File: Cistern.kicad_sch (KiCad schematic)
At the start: 15 parts, among them J2 Gauge Stepper, J3 Power Connector, Q1 IRF9540N, SW1 WiFi reset switch, SW2 Water Sensor, U1 ULN2003A, U3 Boost Converter (5->20 V)

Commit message: Changing schematic to fit parts and starting PCB design
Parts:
- removed Q1: IRF9540N, Package_TO_SOT_THT:TO-220-3_Vertical, symbol Transistor_FET:IRF9540N
- added Q1: BD244C, Package_TO_SOT_THT:TO-220-3_Vertical, symbol Device:Q_PNP_BCE
- D1: footprint LED_THT:LED_D4.0mm -> LED_THT:LED_D5.0mm
- R1: value 250 -> 150
- R2: value 200k -> 68
- R4: value 160 -> 150
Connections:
- net +5V: now also U1.9 (COM), Q1.3 (E); no longer R2.1
- net GND: no longer U1.9 (COM)
- net at J2.1 (Pin_1): now also U1.15 (O2); no longer U1.16 (O1)
- net at J2.2 (Pin_2): now also U1.14 (O3); no longer U1.15 (O2)
- net at J2.3 (Pin_3): now also U1.13 (O4); no longer U1.14 (O3)
- net at J2.4 (Pin_4): now also U1.12 (O5); no longer U1.13 (O4)
- net at U1.1 (I1): now also MCU1.5 (GPIO35); no longer MCU1.10 (GPIO27)
- net at D1.1 (K), R3.1: now also U1.11 (O6); no longer U1.10 (O7)
- net at R2.2: now also U1.16 (O1); no longer U1.11 (O6)
- net at U1.2 (I2): now also MCU1.6 (GPIO32); no longer MCU1.9 (GPIO26)
- net at U1.3 (I3): now also MCU1.7 (GPIO33); no longer MCU1.8 (GPIO25)
- net at U1.4 (I4): now also MCU1.8 (GPIO25); no longer MCU1.7 (GPIO33)
- net at U1.5 (I5): now also MCU1.9 (GPIO26)
- net at U1.6 (I6): now also MCU1.10 (GPIO27); no longer MCU1.6 (GPIO32)
- net at U1.7 (I7): no longer MCU1.5 (GPIO35)
- net at U3.2 (SW): now also Q1.2 (C)
- new net: Q1.1 (B), R2.1
- no-connect marks 0 -> 20
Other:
- moved on the sheet: D1, J2, R3, R4

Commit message: Working on board layout
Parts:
- removed R3: Alarm Buzzer, symbol Device:R
- added BZ1: Buzzer, Cistern:AZDelivery_KY-012_Buzzer, symbol Device:Buzzer
- D2, SW2: footprint TerminalBlock:TerminalBlock_bornier-2_P5.08mm -> Connector_PinHeader_2.54mm:PinHeader_1x02_P2.54mm_Vertical
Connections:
- net +5V: now also BZ1.1 (+)
- net at D1.1 (K), U1.11 (O6): now also BZ1.2 (-)
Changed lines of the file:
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@@
 	(wire
 		(pts
-			(xy 142.24 82.55) (xy 132.08 82.55)
+			(xy 132.08 81.28) (xy 143.51 81.28)
 		)
 		(stroke
@@
 	(wire
 		(pts
-			(xy 132.08 82.55) (xy 132.08 76.2)
+			(xy 132.08 81.28) (xy 132.08 76.2)
 		)
 		(stroke
@@
 	(wire
 		(pts
-			(xy 160.02 82.55) (xy 160.02 76.2)
+			(xy 160.02 81.28) (xy 160.02 76.2)
 		)
 		(stroke
@@
 	(wire
 		(pts
+			(xy 148.59 81.28) (xy 160.02 81.28)
+		)
+		(stroke
+			(width 0)
+			(type default)
+		)
+	)
+	(wire
+		(pts
 			(xy 110.49 105.41) (xy 96.52 105.41)
 		)
@@
 		(pts
 			(xy 191.77 110.49) (xy 191.77 107.95)
-		)
-		(stroke
-			(width 0)
-			(type default)
-		)
-	)
-	(wire
-		(pts
-			(xy 149.86 82.55) (xy 160.02 82.55)
 		)
 		(stroke
@@
 			)
 		)
-		(property "Footprint" "TerminalBlock:TerminalBlock_bornier-2_P5.08mm"
+		(property "Footprint" "Connector_PinHeader_2.54mm:PinHeader_1x02_P2.54mm_Vertical"
 			(at 162.56 125.73 0)
 			(effects
@@
 	)
 	(symbol
+		(lib_id "Device:Buzzer")
+		(at 146.05 83.82 270)
+		(unit 1)
+		(exclude_from_sim no)
+		(in_bom yes)
+		(on_board yes)
+		(dnp no)
+		(fields_autoplaced yes)
+		(property "Reference" "BZ1"
+			(at 149.86 83.305 90)
+			(effects
+				(font
+					(size 1.27 1.27)
+				)
+				(justify left)
+			)
+		)
+		(property "Value" "Buzzer"
+			(at 149.86 85.845 90)
+			(effects
+				(font
+					(size 1.27 1.27)
+				)
+				(justify left)
+			)
+		)
+		(property "Footprint" "Cistern:AZDelivery_KY-012_Buzzer"
+			(at 148.59 83.185 90)
+			(effects
+				(font
+					(size 1.27 1.27)
+				)
+				(hide yes)
+			)
+		)
+		(property "Datasheet" "~"
+			(at 148.59 83.185 90)
+			(effects
+				(font
+					(size 1.27 1.27)
+				)
+				(hide yes)
+			)
+		)
+		(property "Description" "Buzzer, polarized"
+			(at 146.05 83.82 0)
+			(effects
+				(font
+					(size 1.27 1.27)
+				)
+				(hide yes)
+			)
+		)
+		(pin "1"
+		)
+		(pin "2"
+		)
+		(instances
+			(project ""
+				(path "/387a1b1b-4d04-4a4f-a341-bb26b6058549"
+					(reference "BZ1")
+					(unit 1)
+				)
+			)
+		)
+	)
+	(symbol
 		(lib_id "Connector:Jack-DC")
 		(at 54.61 163.83 90)
@@
 			)
 		)
-		(property "Footprint" "TerminalBlock:TerminalBlock_bornier-2_P5.08mm"
+		(property "Footprint" "Connector_PinHeader_2.54mm:PinHeader_1x02_P2.54mm_Vertical"
 			(at 191.77 104.013 0)
 			(effects
@@
 					(unit 1)
 				)
-			)
-		)
-	)
-	(symbol
-		(lib_id "Device:R")
-		(at 146.05 82.55 90)
-		(mirror x)
-		(unit 1)
-		(exclude_from_sim no)
-		(in_bom yes)
-		(on_board yes)
-		(dnp no)
-		(property "Reference" "R3"
-			(at 146.05 88.9 90)
-			(effects
-				(font
-					(size 1.27 1.27)
-				)
-			)
-		)
-		(property "Value" "Alarm Buzzer"
-			(at 146.05 86.36 90)
-			(effects
-				(font
-					(size 1.27 1.27)
-				)
-			)
-		)
-		(property "Footprint" ""
-			(at 146.05 80.772 90)
-			(effects
-				(font
-					(size 1.27 1.27)
-				)
-				(hide yes)
-			)
-		)
-		(property "Datasheet" "~"
-			(at 146.05 82.55 0)
-			(effects
-				(font
-					(size 1.27 1.27)
-				)
-				(hide yes)
-			)
-		)
-		(property "Description" "Resistor"
-			(at 146.05 82.55 0)
-			(effects
-				(font
-					(size 1.27 1.27)
-				)
-				(hide yes)
-			)
-		)
-		(pin "1"
-		)
-		(pin "2"
-		)
-		(instances
-			(project ""
-				(path "/387a1b1b-4d04-4a4f-a341-bb26b6058549"
-					(reference "R3")
-					(unit 1)
-				)

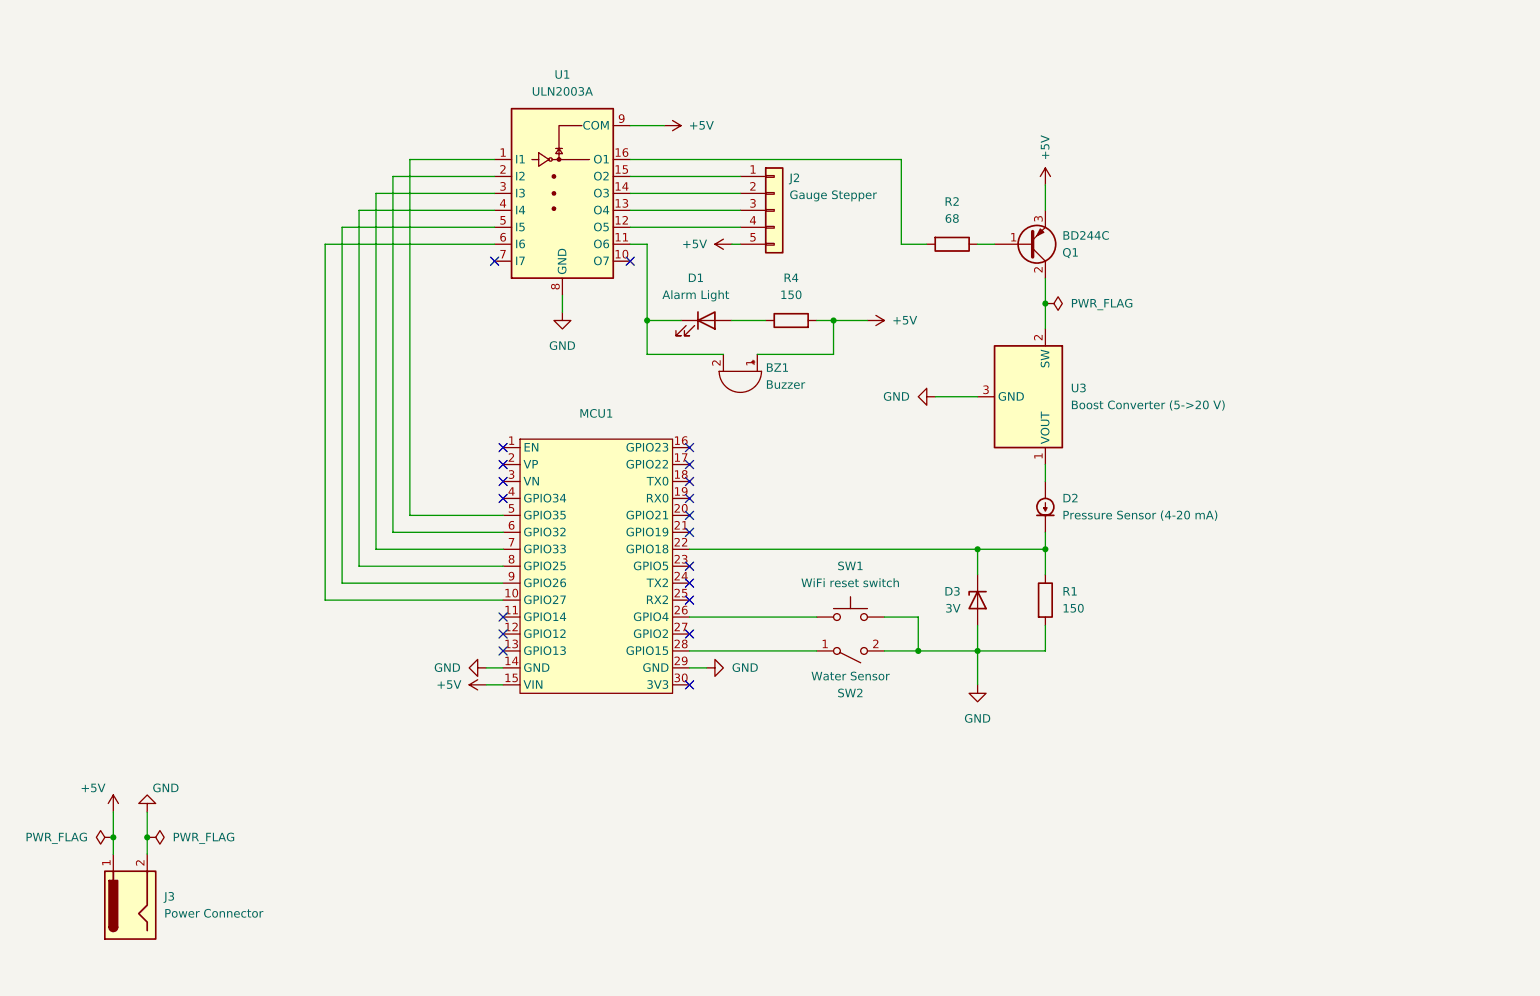
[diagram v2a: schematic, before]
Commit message: Finishing hole-grid ready PCB design
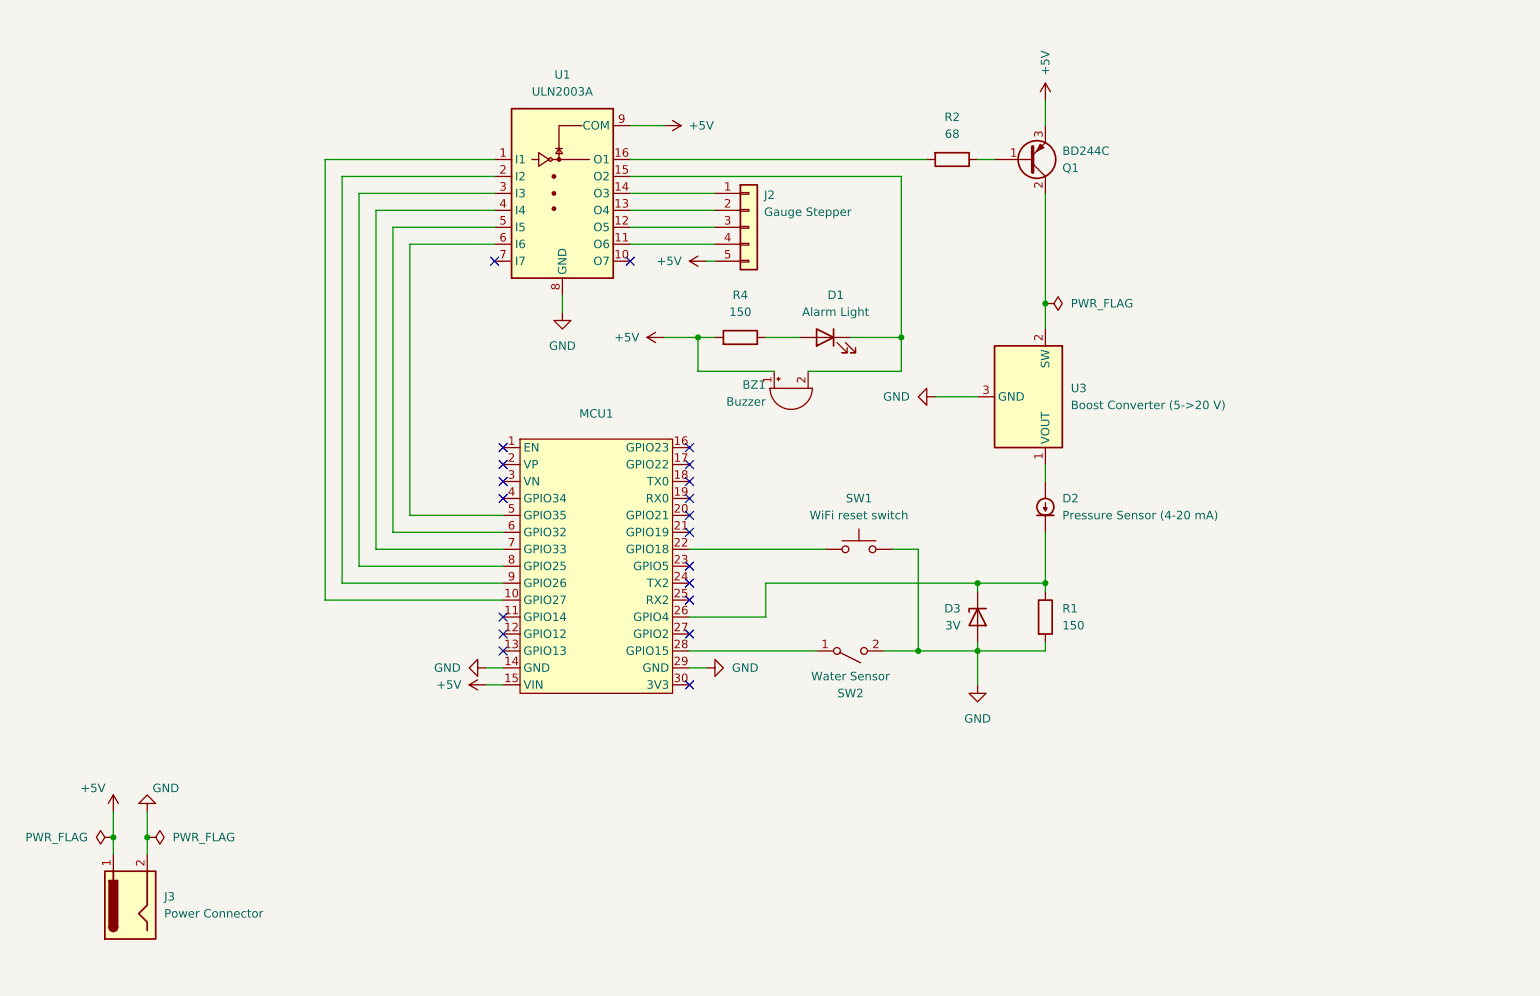
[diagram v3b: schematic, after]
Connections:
- net at J2.1 (Pin_1): now also U1.14 (O3); no longer U1.15 (O2)
- net at J2.2 (Pin_2): now also U1.13 (O4); no longer U1.14 (O3)
- net at J2.3 (Pin_3): now also U1.12 (O5); no longer U1.13 (O4)
- net at J2.4 (Pin_4): now also U1.11 (O6); no longer U1.12 (O5)
- net at U1.1 (I1): now also MCU1.10 (GPIO27); no longer MCU1.5 (GPIO35)
- net at BZ1.2 (-), D1.1 (K): now also U1.15 (O2); no longer U1.11 (O6)
- net at U1.2 (I2): now also MCU1.9 (GPIO26); no longer MCU1.6 (GPIO32)
- net at U1.3 (I3): now also MCU1.8 (GPIO25); no longer MCU1.7 (GPIO33)
- net at U1.4 (I4): now also MCU1.7 (GPIO33); no longer MCU1.8 (GPIO25)
- net at U1.5 (I5): now also MCU1.6 (GPIO32); no longer MCU1.9 (GPIO26)
- net at U1.6 (I6): now also MCU1.5 (GPIO35); no longer MCU1.10 (GPIO27)
- net at D2.1 (K), D3.1 (K), R1.1: now also MCU1.26 (GPIO4); no longer MCU1.22 (GPIO18)
- net at SW1.1: now also MCU1.22 (GPIO18); no longer MCU1.26 (GPIO4)
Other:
- moved on the sheet: BZ1, D1, D3, J2, Q1, R1, R2, R4, SW1

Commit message: Changing pin assignments to make things work
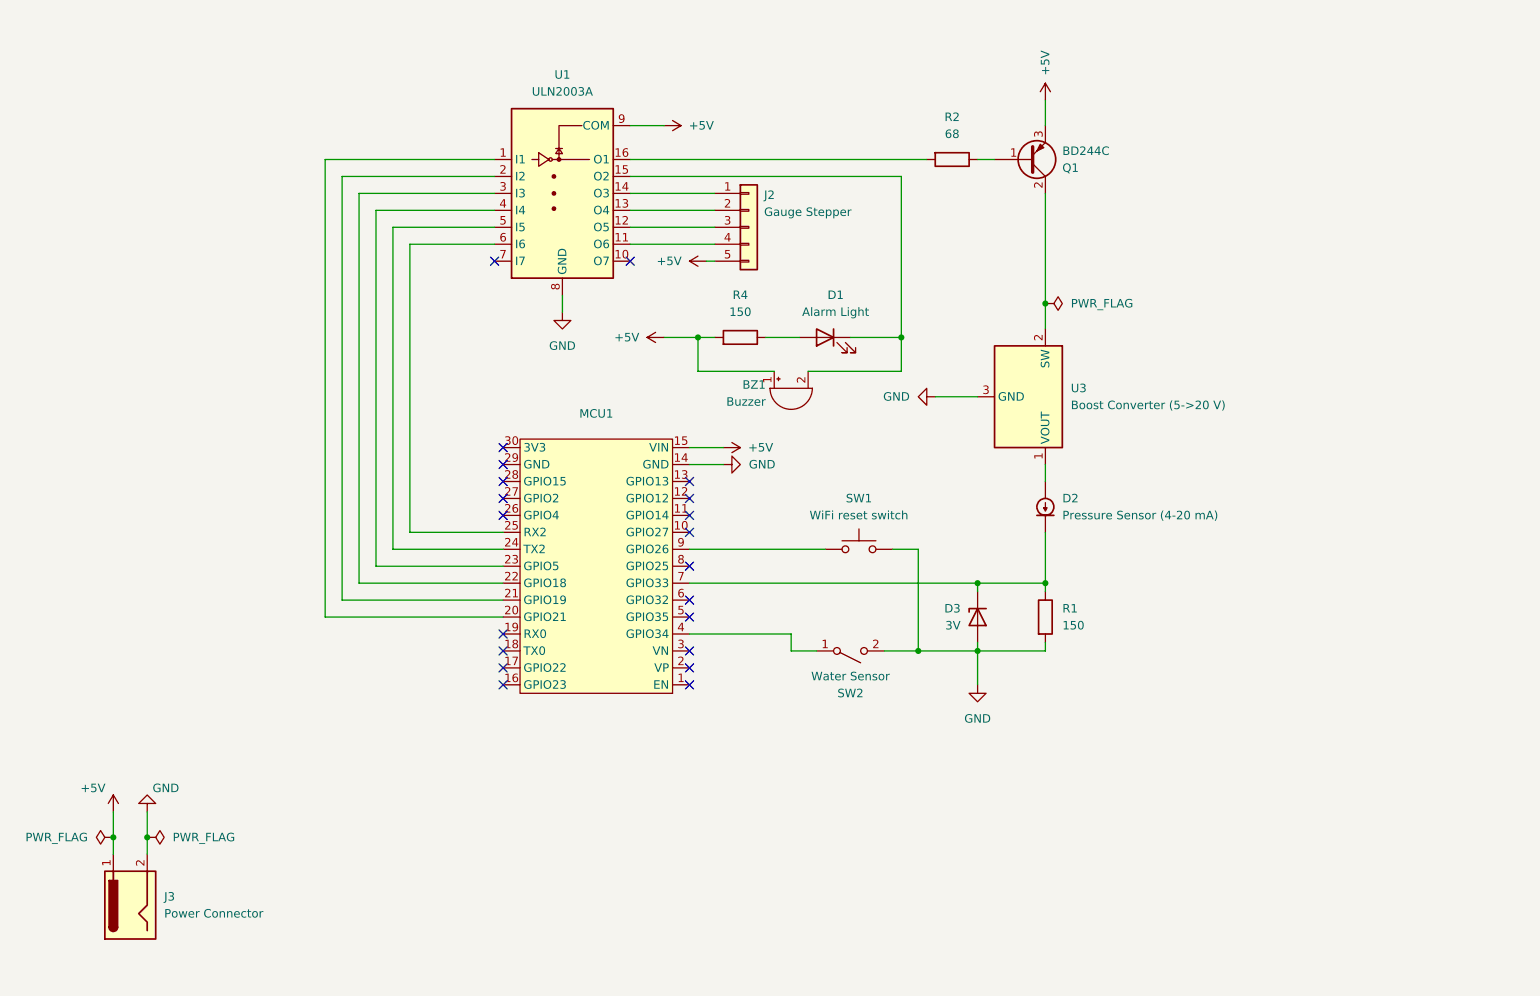
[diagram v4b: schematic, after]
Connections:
- net GND: no longer MCU1.29 (GND)
- net at U1.1 (I1): now also MCU1.20 (GPIO21); no longer MCU1.10 (GPIO27)
- net at U1.2 (I2): now also MCU1.21 (GPIO19); no longer MCU1.9 (GPIO26)
- net at U1.3 (I3): now also MCU1.22 (GPIO18); no longer MCU1.8 (GPIO25)
- net at U1.4 (I4): now also MCU1.23 (GPIO5); no longer MCU1.7 (GPIO33)
- net at U1.5 (I5): now also MCU1.24 (TX2); no longer MCU1.6 (GPIO32)
- net at U1.6 (I6): now also MCU1.25 (RX2); no longer MCU1.5 (GPIO35)
- net at SW1.1: now also MCU1.9 (GPIO26); no longer MCU1.22 (GPIO18)
- net at D2.1 (K), D3.1 (K), R1.1: now also MCU1.7 (GPIO33); no longer MCU1.26 (GPIO4)
- net at MCU1.28 (GPIO15): no longer SW2.1 (A)
- net at MCU1.4 (GPIO34): now also SW2.1 (A)
- no-connect marks 20 -> 21
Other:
- moved on the sheet: MCU1

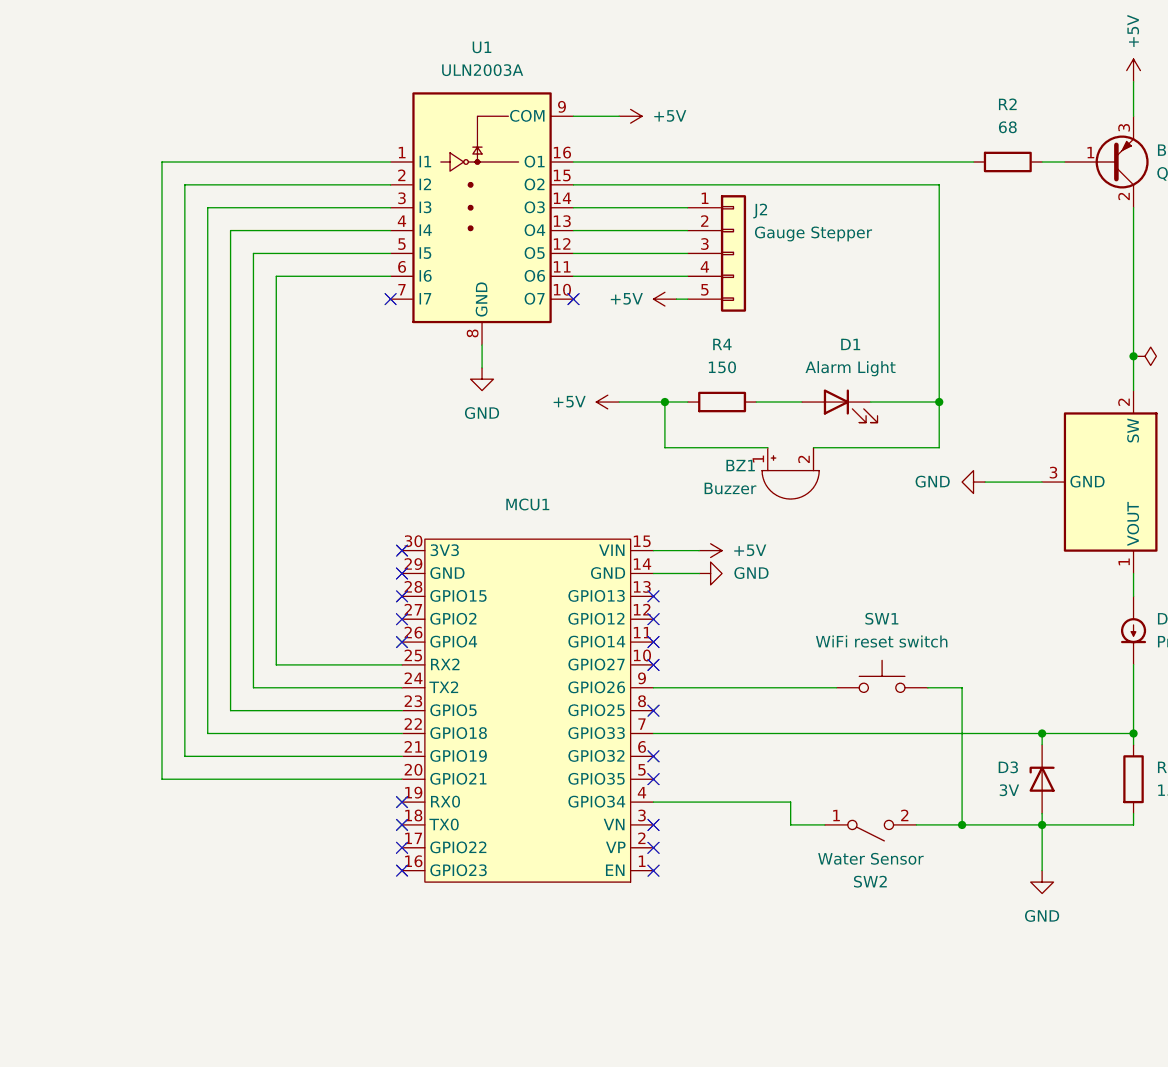
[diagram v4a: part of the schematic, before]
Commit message: Changing assignments some more and updating board design
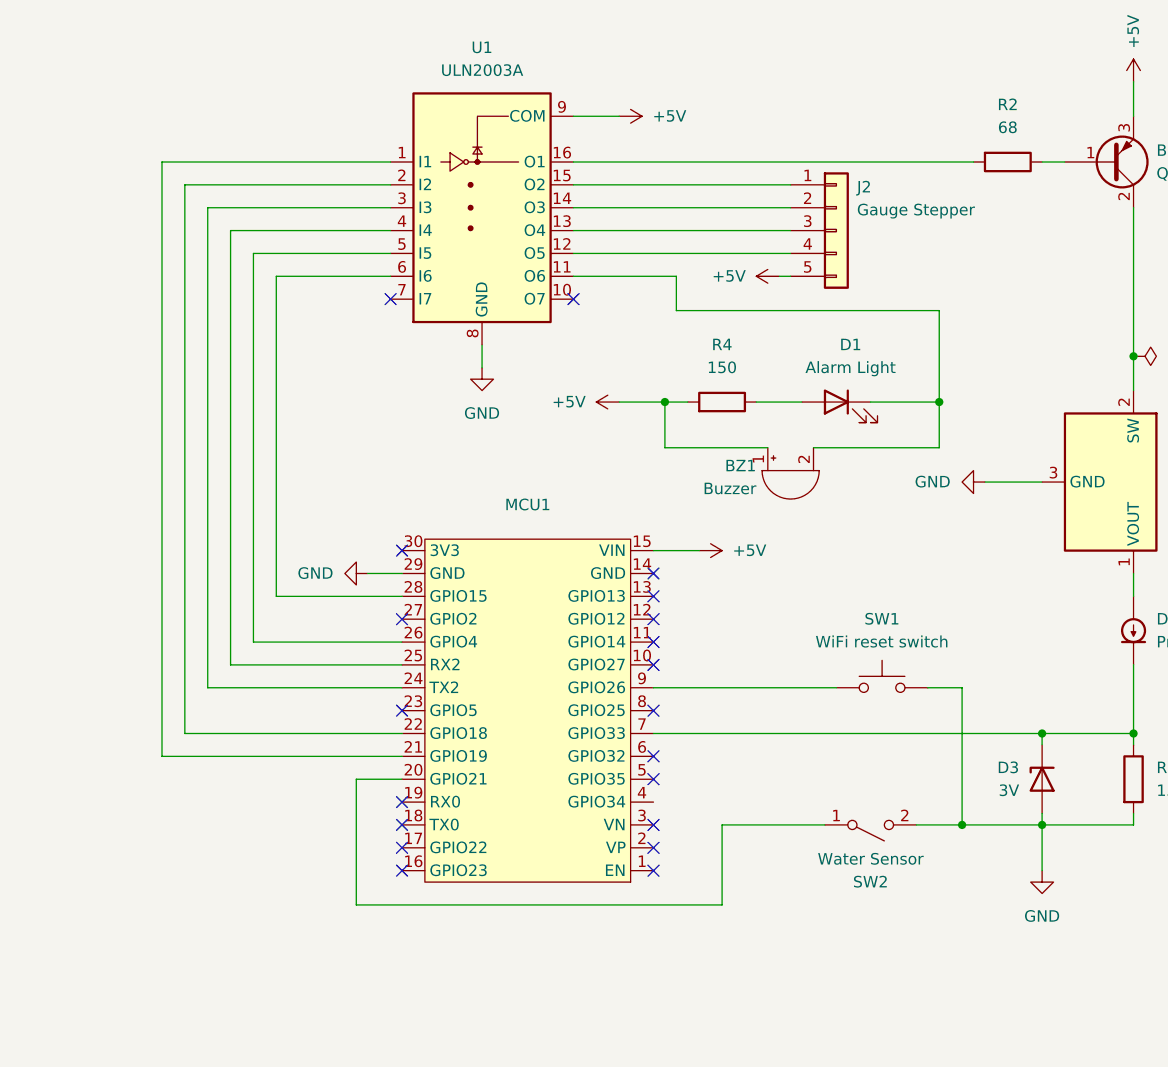
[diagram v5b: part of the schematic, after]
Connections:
- net GND: now also MCU1.29 (GND); no longer MCU1.14 (GND)
- net at J2.1 (Pin_1): now also U1.15 (O2); no longer U1.14 (O3)
- net at J2.2 (Pin_2): now also U1.14 (O3); no longer U1.13 (O4)
- net at J2.3 (Pin_3): now also U1.13 (O4); no longer U1.12 (O5)
- net at J2.4 (Pin_4): now also U1.12 (O5); no longer U1.11 (O6)
- net at U1.1 (I1): now also MCU1.21 (GPIO19); no longer MCU1.20 (GPIO21)
- net at BZ1.2 (-), D1.1 (K): now also U1.11 (O6); no longer U1.15 (O2)
- net at U1.2 (I2): now also MCU1.22 (GPIO18); no longer MCU1.21 (GPIO19)
- net at U1.3 (I3): now also MCU1.24 (TX2); no longer MCU1.22 (GPIO18)
- net at U1.4 (I4): now also MCU1.25 (RX2); no longer MCU1.23 (GPIO5)
- net at U1.5 (I5): now also MCU1.26 (GPIO4); no longer MCU1.24 (TX2)
- net at U1.6 (I6): now also MCU1.28 (GPIO15); no longer MCU1.25 (RX2)
- net at SW2.1 (A): now also MCU1.20 (GPIO21); no longer MCU1.4 (GPIO34)
- no-connect marks 21 -> 20
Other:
- moved on the sheet: J2
